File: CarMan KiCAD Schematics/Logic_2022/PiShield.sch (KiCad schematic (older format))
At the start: 11 parts, among them J2 J2 NI I2C, J3 J3 Logic-TSI, J4 J4 GLV BOB, J6 J6 NI CAN, U10 BNO_055, U11 Raspberry_Pi_RTC, U6 RaspberryPi3

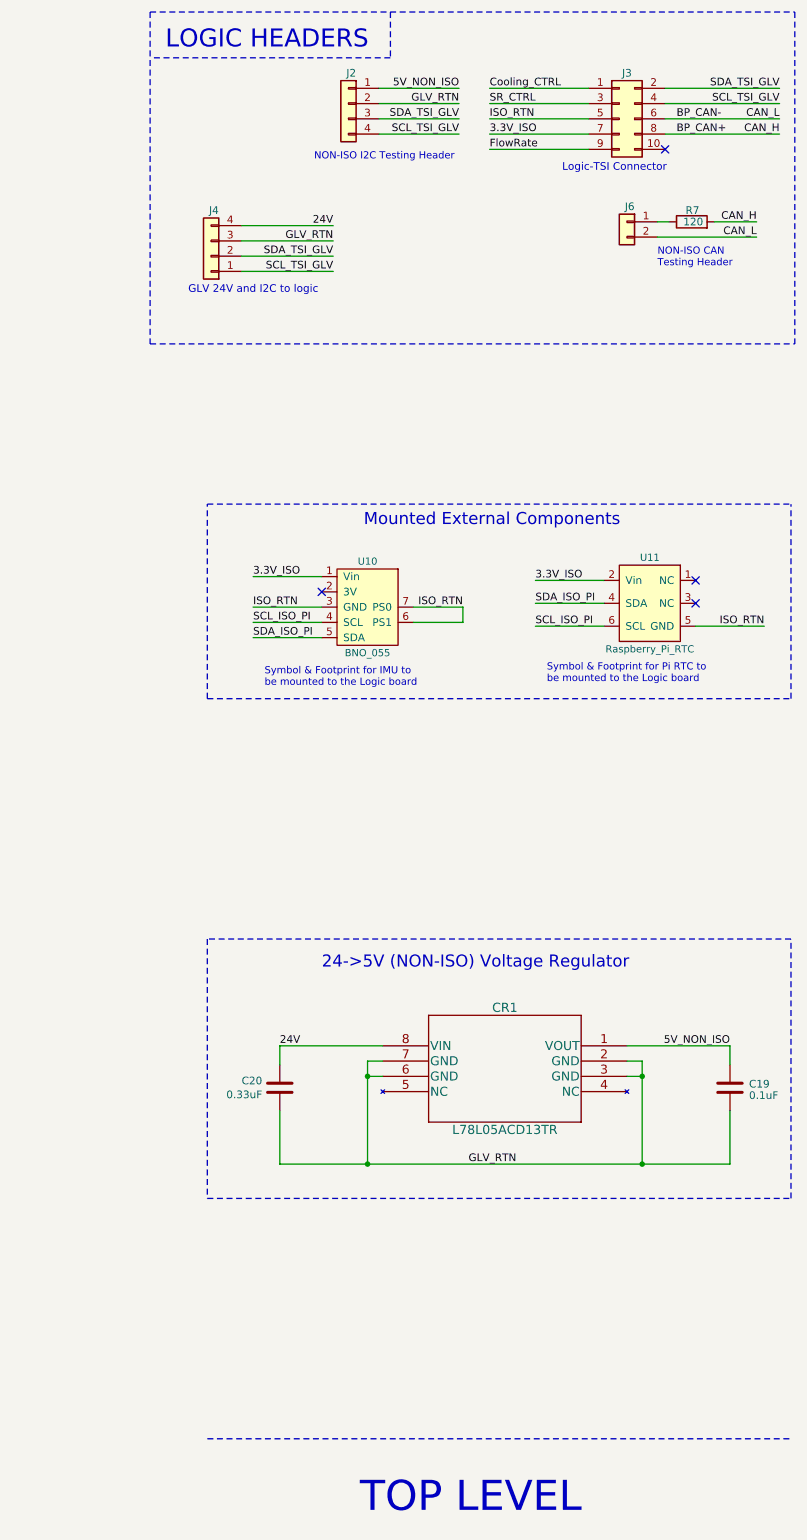
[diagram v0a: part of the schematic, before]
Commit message: Created the Pi Shield schematic and a new library for pican2
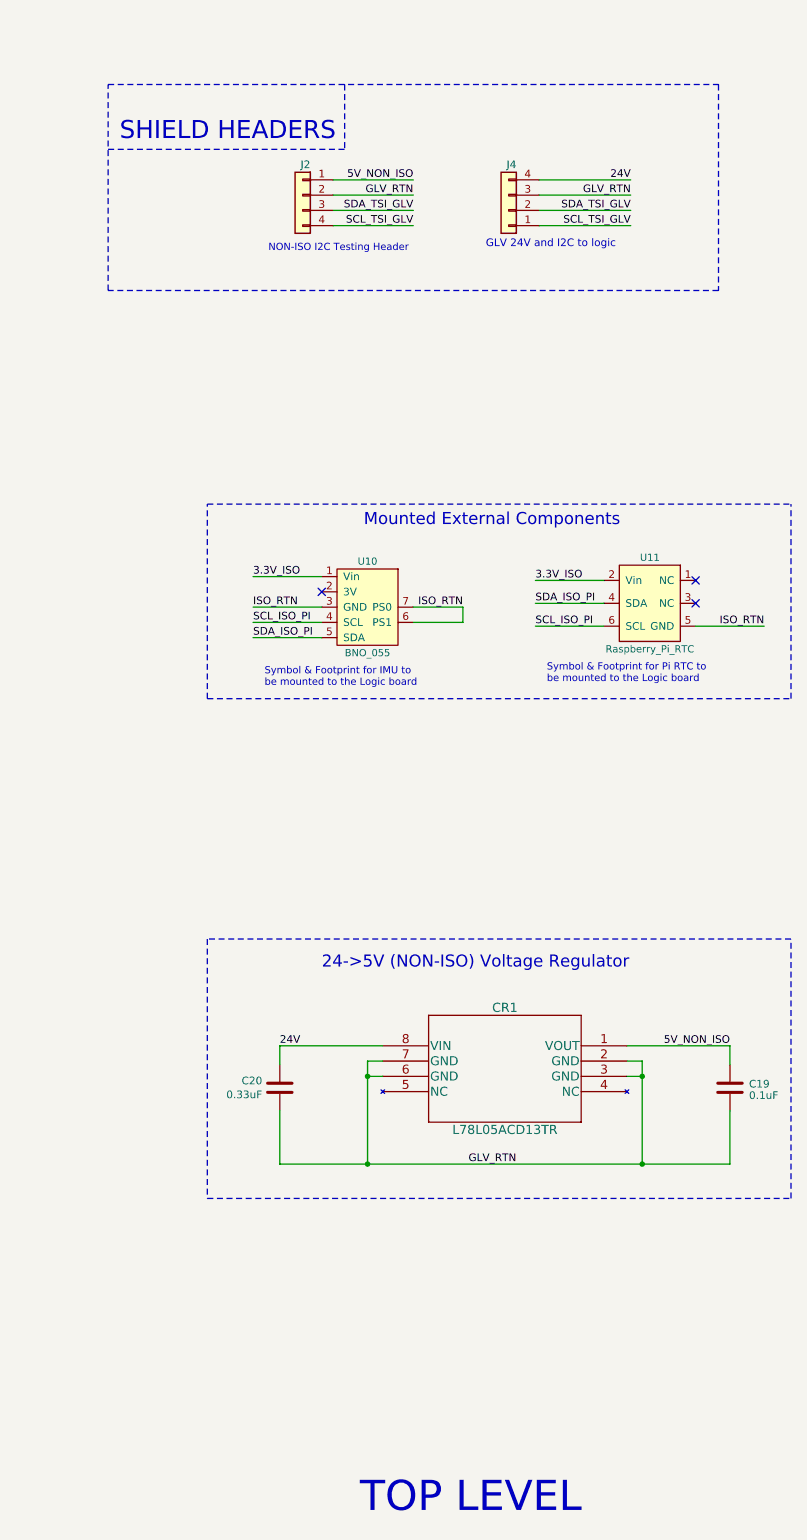
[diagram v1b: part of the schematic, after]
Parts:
- removed J3: J3 Logic-TSI, Connector_PinSocket_2.54mm:PinSocket_2x05_P2.54mm_Vertical, symbol Connector_Generic:Conn_02x05_Odd_Even
- removed J6: J6 NI CAN, Connector_PinSocket_2.54mm:PinSocket_1x02_P2.54mm_Vertical, symbol Connector_Generic:Conn_01x02
- removed R7: 120, Resistor_SMD:R_0805_2012Metric_Pad1.15x1.40mm_HandSolder, symbol Logic-rescue:R-Device-Logic-rescue
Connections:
- no-connect marks 26 -> 25
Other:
- note added: "SHIELD HEADERS"
- note removed: "LOGIC HEADERS"
- note removed: "Logic-TSI Connector"
- note removed: "NON-ISO CAN\nTesting Header"
- moved on the sheet: J2, J4

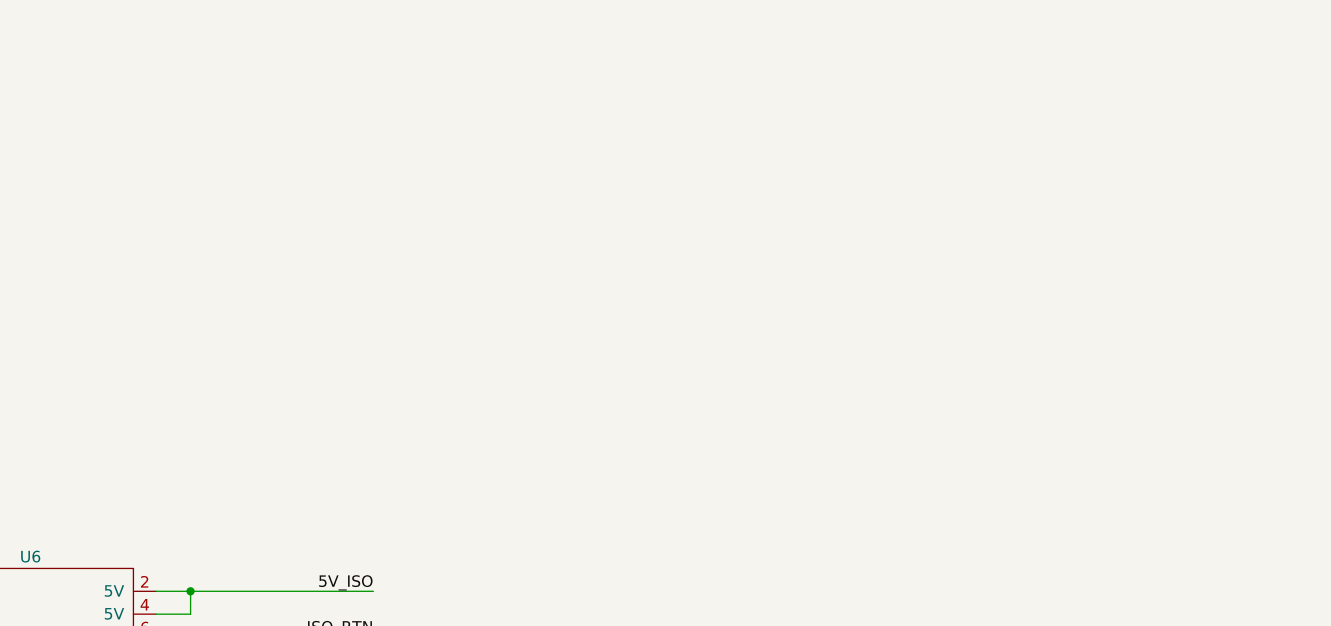
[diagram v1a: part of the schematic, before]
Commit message: Create the regulator circuit based on the P783-S datasheet
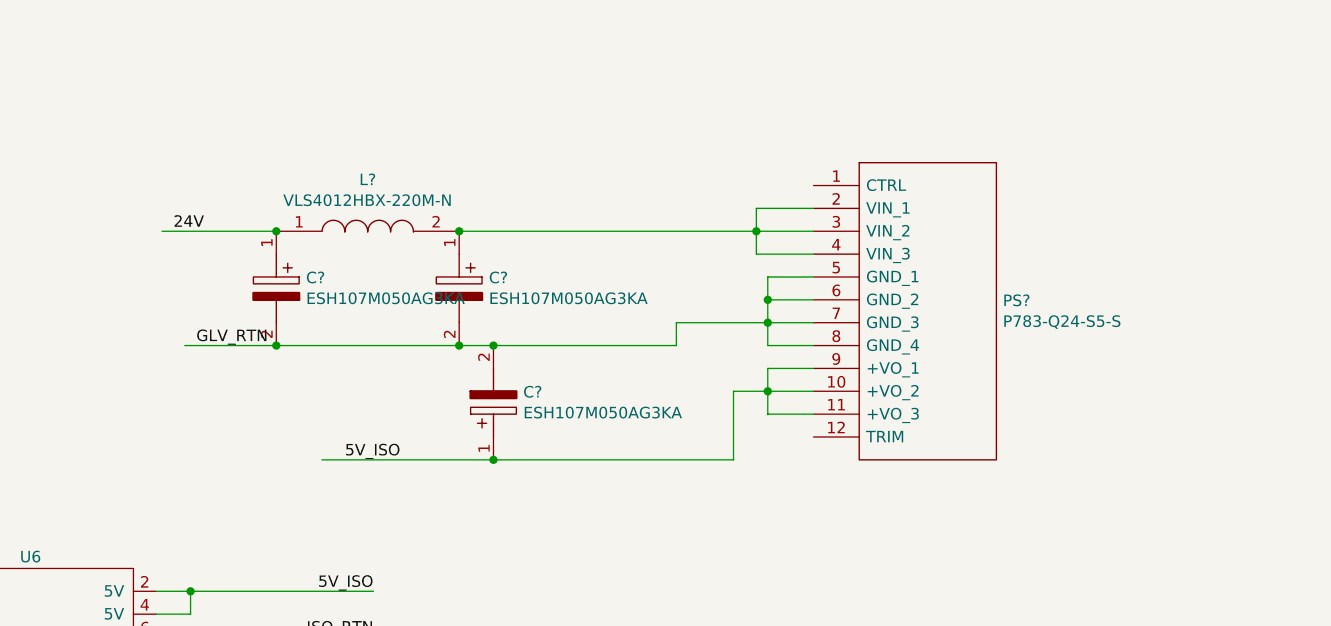
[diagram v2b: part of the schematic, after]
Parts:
- added C? (x3): ESH107M050AG3KA, CAPPRD350W60D800H1250, symbol SamacSys_Parts:ESH107M050AG3KA
- added L?: VLS4012HBX-220M-N, VLS4012HBX220MN, symbol SamacSys_Parts:VLS4012HBX-220M-N
- added PS?: P783-Q24-S5-S, P783Q24S5S, symbol SamacSys_Parts:P783-Q24-S5-S
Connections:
- wire segments 66 -> 95
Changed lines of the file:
@@
 Wire Notes Line
 	13050 1000 13050 1425
+$Comp
+L SamacSys_Parts:P783-Q24-S5-S PS?
+U 1 1 62268053
+P 7650 2850
+F 0 "PS?" H 8478 2346 50  0000 L CNN
+F 1 "P783-Q24-S5-S" H 8478 2255 50  0000 L CNN
+F 2 "P783Q24S5S" H 8500 2950 50  0001 L CNN
+F 3 "https://www.cui.com/product/resource/digikeypdf/p783-s.pdf" H 8500 2850 50  0001 L CNN
+F 4 "Non-Isolated DC/DC Converters 5 Vdc, 3 A, 15 W, 8~36 Vdc Input Range" H 8500 2750 50  0001 L CNN "Description"
+F 5 "15.35" H 8500 2650 50  0001 L CNN "Height"
+F 6 "490-P783-Q24-S5-S" H 8500 2550 50  0001 L CNN "Mouser Part Number"
+F 7 "https://www.mouser.co.uk/ProductDetail/CUI-Inc/P783-Q24-S5-S?qs=sPbYRqrBIVlCN3ziQDuGDA%3D%3D" H 8500 2450 50  0001 L CNN "Mouser Price/Stock"
+F 8 "CUI Inc." H 8500 2350 50  0001 L CNN "Manufacturer_Name"
+F 9 "P783-Q24-S5-S" H 8500 2250 50  0001 L CNN "Manufacturer_Part_Number"
+	1    7650 2850
+	1    0    0    -1
+$EndComp
+Wire Wire Line
+	7650 3250 7450 3250
+Wire Wire Line
+	7450 3350 7650 3350
+Wire Wire Line
+	7650 3450 7450 3450
+Wire Wire Line
+	7450 3250 7450 3350
+Connection ~ 7450 3350
+Wire Wire Line
+	7450 3350 7450 3450
+Wire Wire Line
+	7650 3550 7450 3550
+Wire Wire Line
+	7450 3550 7450 3450
+Connection ~ 7450 3450
+Wire Wire Line
+	7650 2950 7400 2950
+Wire Wire Line
+	7400 2950 7400 3050
+Wire Wire Line
+	7400 3050 7650 3050
+Wire Wire Line
+	7650 3150 7400 3150
+Wire Wire Line
+	7400 3150 7400 3050
+Connection ~ 7400 3050
+Wire Wire Line
+	7650 3650 7450 3650
+Wire Wire Line
+	7450 3650 7450 3750
+Wire Wire Line
+	7450 3750 7650 3750
+Wire Wire Line
+	7650 3850 7450 3850
+Wire Wire Line
+	7450 3850 7450 3750
+Connection ~ 7450 3750
+$Comp
+L SamacSys_Parts:ESH107M050AG3KA C?
+U 1 1 62284A0F
+P 6100 3050
+F 0 "C?" V 6304 3180 50  0000 L CNN
+F 1 "ESH107M050AG3KA" V 6395 3180 50  0000 L CNN
+F 2 "CAPPRD350W60D800H1250" H 6450 3100 50  0001 L CNN
+F 3 "https://connect.kemet.com:7667/gateway/IntelliData-ComponentDocumentation/1.0/download/specsheet/ESH107M050AG3KA" H 6450 3000 50  0001 L CNN
+F 4 "ESH, Aluminum Electrolytic, 100 uF, 20%, 50 VDC, -40/+105C, Lead Spacing = 3.5mm" H 6450 2900 50  0001 L CNN "Description"
+F 5 "12.5" H 6450 2800 50  0001 L CNN "Height"
+F 6 "" H 6450 2700 50  0001 L CNN "Mouser Part Number"
+F 7 "" H 6450 2600 50  0001 L CNN "Mouser Price/Stock"
+F 8 "Kemet" H 6450 2500 50  0001 L CNN "Manufacturer_Name"
+F 9 "ESH107M050AG3KA" H 6450 2400 50  0001 L CNN "Manufacturer_Part_Number"
+	1    6100 3050
+	0    1    1    0
+$EndComp
+$Comp
+L SamacSys_Parts:VLS4012HBX-220M-N L?
+U 1 1 6228A76D
+P 5300 3050
+F 0 "L?" H 5700 3275 50  0000 C CNN
+F 1 "VLS4012HBX-220M-N" H 5700 3184 50  0000 C CNN
+F 2 "VLS4012HBX220MN" H 5950 3100 50  0001 L CNN
+F 3 "https://product.tdk.com/system/files/dam/doc/product/inductor/inductor/smd/catalog/inductor_commercial_power_vls4012hbx-n_en.pdf" H 5950 3000 50  0001 L CNN
+F 4 "SMD / SMT Inductors (Coils), L=22?H, L x W x T :" H 5950 2900 50  0001 L CNN "Description"
+F 5 "1.2" H 5950 2800 50  0001 L CNN "Height"
+F 6 "810-VLS4012HBX220M-N" H 5950 2700 50  0001 L CNN "Mouser Part Number"
+F 7 "https://www.mouser.co.uk/ProductDetail/TDK/VLS4012HBX-220M-N?qs=A6eO%252BMLsxmR3U%2FS6%252BaW3qw%3D%3D" H 5950 2600 50  0001 L CNN "Mouser Price/Stock"
+F 8 "TDK" H 5950 2500 50  0001 L CNN "Manufacturer_Name"
+F 9 "VLS4012HBX-220M-N" H 5950 2400 50  0001 L CNN "Manufacturer_Part_Number"
+	1    5300 3050
+	1    0    0    -1
+$EndComp
+$Comp
+L SamacSys_Parts:ESH107M050AG3KA C?
+U 1 1 6228C858
+P 5300 3050
+F 0 "C?" V 5504 3180 50  0000 L CNN
+F 1 "ESH107M050AG3KA" V 5595 3180 50  0000 L CNN
+F 2 "CAPPRD350W60D800H1250" H 5650 3100 50  0001 L CNN
+F 3 "https://connect.kemet.com:7667/gateway/IntelliData-ComponentDocumentation/1.0/download/specsheet/ESH107M050AG3KA" H 5650 3000 50  0001 L CNN
+F 4 "ESH, Aluminum Electrolytic, 100 uF, 20%, 50 VDC, -40/+105C, Lead Spacing = 3.5mm" H 5650 2900 50  0001 L CNN "Description"
+F 5 "12.5" H 5650 2800 50  0001 L CNN "Height"
+F 6 "" H 5650 2700 50  0001 L CNN "Mouser Part Number"
+F 7 "" H 5650 2600 50  0001 L CNN "Mouser Price/Stock"
+F 8 "Kemet" H 5650 2500 50  0001 L CNN "Manufacturer_Name"
+F 9 "ESH107M050AG3KA" H 5650 2400 50  0001 L CNN "Manufacturer_Part_Number"
+	1    5300 3050
+	0    1    1    0
+$EndComp
+Wire Wire Line
+	7400 3050 6100 3050
+Connection ~ 6100 3050
+Connection ~ 5300 3050
+Text Label 4850 3050 0    50   ~ 0
+24V
+Wire Wire Line
+	4800 3050 5300 3050
+Wire Wire Line
+	7050 3450 7050 3550
+Wire Wire Line
+	5300 3550 6100 3550
+Connection ~ 6100 3550
+Wire Wire Line
+	5300 3550 4900 3550
+Connection ~ 5300 3550
+Wire Wire Line
+	7450 3450 7050 3450
+Text Label 4950 3550 0    50   ~ 0
+GLV_RTN
+Wire Wire Line
+	7050 3550 6250 3550
+$Comp
+L SamacSys_Parts:ESH107M050AG3KA C?
+U 1 1 622A6061
+P 6250 4050
+F 0 "C?" V 6546 3920 50  0000 R CNN
+F 1 "ESH107M050AG3KA" V 6455 3920 50  0000 R CNN
+F 2 "CAPPRD350W60D800H1250" H 6600 4100 50  0001 L CNN
+F 3 "https://connect.kemet.com:7667/gateway/IntelliData-ComponentDocumentation/1.0/download/specsheet/ESH107M050AG3KA" H 6600 4000 50  0001 L CNN
+F 4 "ESH, Aluminum Electrolytic, 100 uF, 20%, 50 VDC, -40/+105C, Lead Spacing = 3.5mm" H 6600 3900 50  0001 L CNN "Description"
+F 5 "12.5" H 6600 3800 50  0001 L CNN "Height"
+F 6 "" H 6600 3700 50  0001 L CNN "Mouser Part Number"
+F 7 "" H 6600 3600 50  0001 L CNN "Mouser Price/Stock"
+F 8 "Kemet" H 6600 3500 50  0001 L CNN "Manufacturer_Name"
+F 9 "ESH107M050AG3KA" H 6600 3400 50  0001 L CNN "Manufacturer_Part_Number"
+	1    6250 4050
+	0    -1   -1   0
+$EndComp
+Connection ~ 6250 3550
+Wire Wire Line
+	6250 3550 6100 3550
+Wire Wire Line
+	7450 3750 7300 3750
+Wire Wire Line
+	7300 3750 7300 4050
+Wire Wire Line
+	7300 4050 6250 4050
+Wire Wire Line
+	6250 4050 5500 4050
+Connection ~ 6250 4050
+Text Label 5600 4050 0    50   ~ 0
+5V_ISO
 $EndSCHEMATC
